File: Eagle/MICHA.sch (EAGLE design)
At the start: 57 parts, among them IC1 LM4041A12LP, K1 PIN20X2, T1 BSS84, U1 ARDUINO_MKR_ZERO, U2 MIKROE_CLICK, X1 RJ45-RJULE4318101, X2 RJ45-RJULE4318101, X3 RJ45-RJULE4318101, X4 RJ45-RJULE4318101, X5 RJ45-RJULE4318101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

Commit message: Downgrade to current version of PCB
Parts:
- R6, R7: value 15-1/4W -> 2k
- Z1, Z2: value 5,1V-1W -> 5,1V/1W
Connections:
- net SOL_HOT renamed SOL_WARM
- net VALVE1_DIR renamed VALVE1_CLOSE
- net VALVE1_POWER renamed VALVE1_OPEN
- net VALVE2_DIR renamed VALVE2_CLOSE
- net VALVE2_POWER renamed VALVE2_OPEN
- net D0: now also TBD2.6; no longer TBD2.4
- net D19: now also U1.A4; no longer U1.A1
- net D2: now also TBD2.4; no longer TBD2.6
- net D21: now also U1.A6; no longer U1.DAC0/A0
- net N$14: now also U1.A5; no longer U1.A2
- net THERMI1: now also U1.DAC0/A0; no longer U1.A3
- net THERMI2: now also U1.A1; no longer U1.A4
- net THERMI3: now also U1.A2; no longer U1.A5
- net THERMI4: now also U1.A3; no longer U1.A6
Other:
- moved on the sheet: AN, C1, C10, C11, C12, C13, C14, C15, C2, C3, C4, C5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

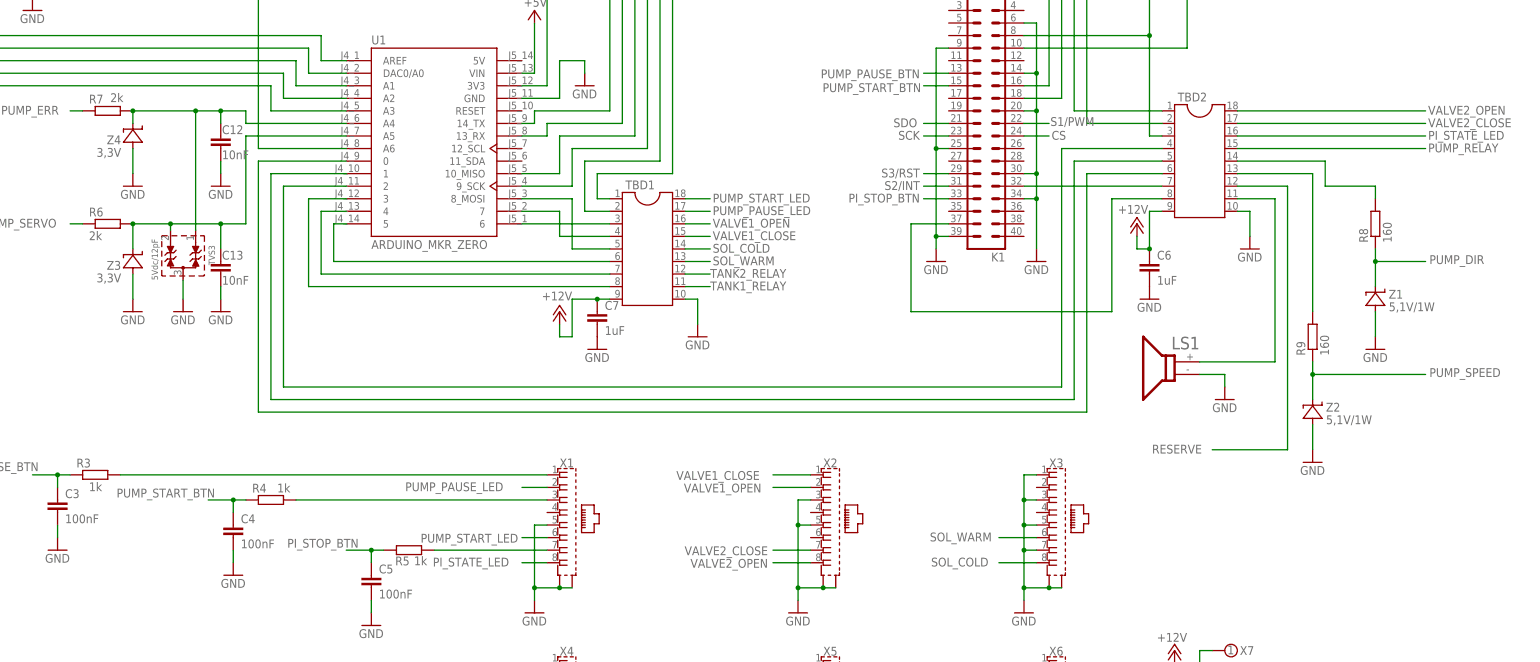
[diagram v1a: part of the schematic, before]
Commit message: Speed and power pump pins modified
- Voltage tags on X7
- Output valve names updated
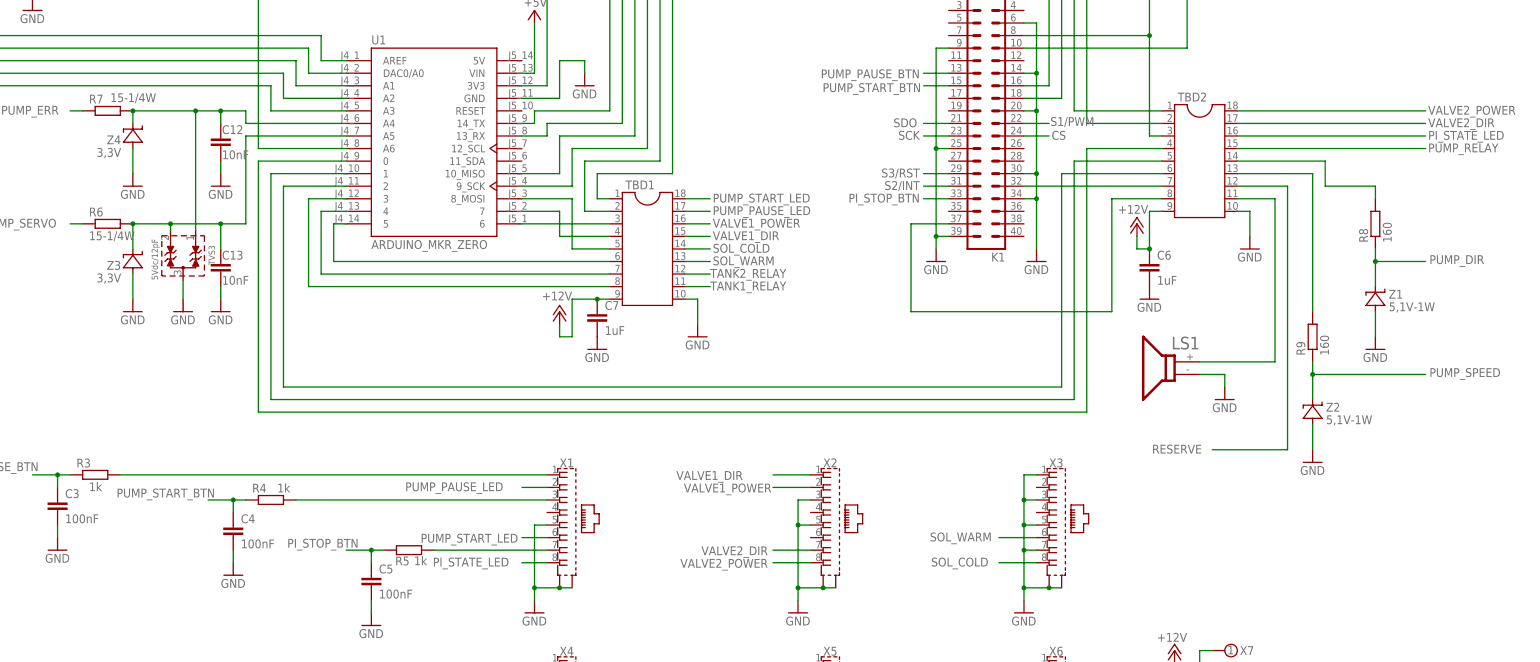
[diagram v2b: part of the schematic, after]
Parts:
- R6, R7: value 2k -> 15-1/4W
- Z1, Z2: value 5,1V/1W -> 5,1V-1W
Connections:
- net VALVE1_CLOSE renamed VALVE1_DIR
- net VALVE1_OPEN renamed VALVE1_POWER
- net VALVE2_CLOSE renamed VALVE2_DIR
- net VALVE2_OPEN renamed VALVE2_POWER
- net D0: now also TBD2.4; no longer TBD2.6
- net D2: now also TBD2.6; no longer TBD2.4
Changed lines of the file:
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@@
 <part name="GND9" library="supply1" deviceset="GND" device=""/>
 <part name="P+2" library="supply1" library_urn="urn:adsk.eagle:library:371" deviceset="+12V" device=""/>
-<part name="R6" library="resistor" deviceset="R-EU_" device="R1206" value="2k"/>
-<part name="R7" library="resistor" deviceset="R-EU_" device="R1206" value="2k"/>
+<part name="R6" library="resistor" deviceset="R-EU_" device="R1206" value="15-1/4W"/>
+<part name="R7" library="resistor" deviceset="R-EU_" device="R1206" value="15-1/4W"/>
 <part name="TBD2" library="ic-package" library_urn="urn:adsk.eagle:library:239" deviceset="DIL18" device="S" package3d_urn="urn:adsk.eagle:package:14434/1"/>
 <part name="GND12" library="supply1" deviceset="GND" device=""/>
@@
 <part name="GND39" library="supply1" deviceset="GND" device=""/>
 <part name="GND10" library="supply1" deviceset="GND" device=""/>
-<part name="Z1" library="Zener_SMA" deviceset="ZENER_SMA" device="" value="5,1V/1W"/>
-<part name="Z2" library="Zener_SMA" deviceset="ZENER_SMA" device="" value="5,1V/1W"/>
+<part name="Z1" library="Zener_SMA" deviceset="ZENER_SMA" device="" value="5,1V-1W"/>
+<part name="Z2" library="Zener_SMA" deviceset="ZENER_SMA" device="" value="5,1V-1W"/>
 <part name="Z3" library="Zener_SMA" deviceset="ZENER_SMA" device="" value="3,3V"/>
 <part name="Z4" library="Zener_SMA" deviceset="ZENER_SMA" device="" value="3,3V"/>
@@
 </segment>
 </net>
-<net name="VALVE1_OPEN" class="0">
+<net name="VALVE1_POWER" class="0">
 <segment>
 <wire x1="238.76" y1="106.68" x2="231.14" y2="106.68" width="0.1524" layer="91"/>
@@
 </segment>
 </net>
-<net name="VALVE1_CLOSE" class="0">
+<net name="VALVE1_DIR" class="0">
 <segment>
 <wire x1="238.76" y1="109.22" x2="231.14" y2="109.22" width="0.1524" layer="91"/>
@@
 </segment>
 </net>
-<net name="VALVE2_OPEN" class="0">
+<net name="VALVE2_POWER" class="0">
 <segment>
 <label x="363.728" y="182.118" size="1.778" layer="95"/>
@@
 </segment>
 </net>
-<net name="VALVE2_CLOSE" class="0">
+<net name="VALVE2_DIR" class="0">
 <segment>
 <label x="363.728" y="179.578" size="1.778" layer="95"/>
@@
 <pinref part="U1" gate="G$1" pin="0"/>
 <wire x1="127" y1="172.72" x2="144.78" y2="172.72" width="0.1524" layer="91"/>
-<pinref part="TBD2" gate="G$1" pin="6"/>
-<wire x1="309.88" y1="170.18" x2="294.64" y2="170.18" width="0.1524" layer="91"/>
-<wire x1="294.64" y1="170.18" x2="294.64" y2="121.92" width="0.1524" layer="91"/>
+<wire x1="294.64" y1="175.26" x2="294.64" y2="121.92" width="0.1524" layer="91"/>
+<pinref part="TBD2" gate="G$1" pin="4"/>
+<wire x1="294.64" y1="175.26" x2="309.88" y2="175.26" width="0.1524" layer="91"/>
 </segment>
 </net>
@@
 <pinref part="U1" gate="G$1" pin="2"/>
 <wire x1="132.08" y1="167.64" x2="144.78" y2="167.64" width="0.1524" layer="91"/>
-<pinref part="TBD2" gate="G$1" pin="4"/>
-<wire x1="309.88" y1="175.26" x2="289.56" y2="175.26" width="0.1524" layer="91"/>
-<wire x1="289.56" y1="175.26" x2="289.56" y2="127" width="0.1524" layer="91"/>
-</segment>
-</net>
+<wire x1="289.56" y1="127" x2="289.56" y2="170.18" width="0.1524" layer="91"/>
+<pinref part="TBD2" gate="G$1" pin="6"/>
+<wire x1="289.56" y1="170.18" x2="309.88" y2="170.18" width="0.1524" layer="91"/>
+</segment>
+</net>

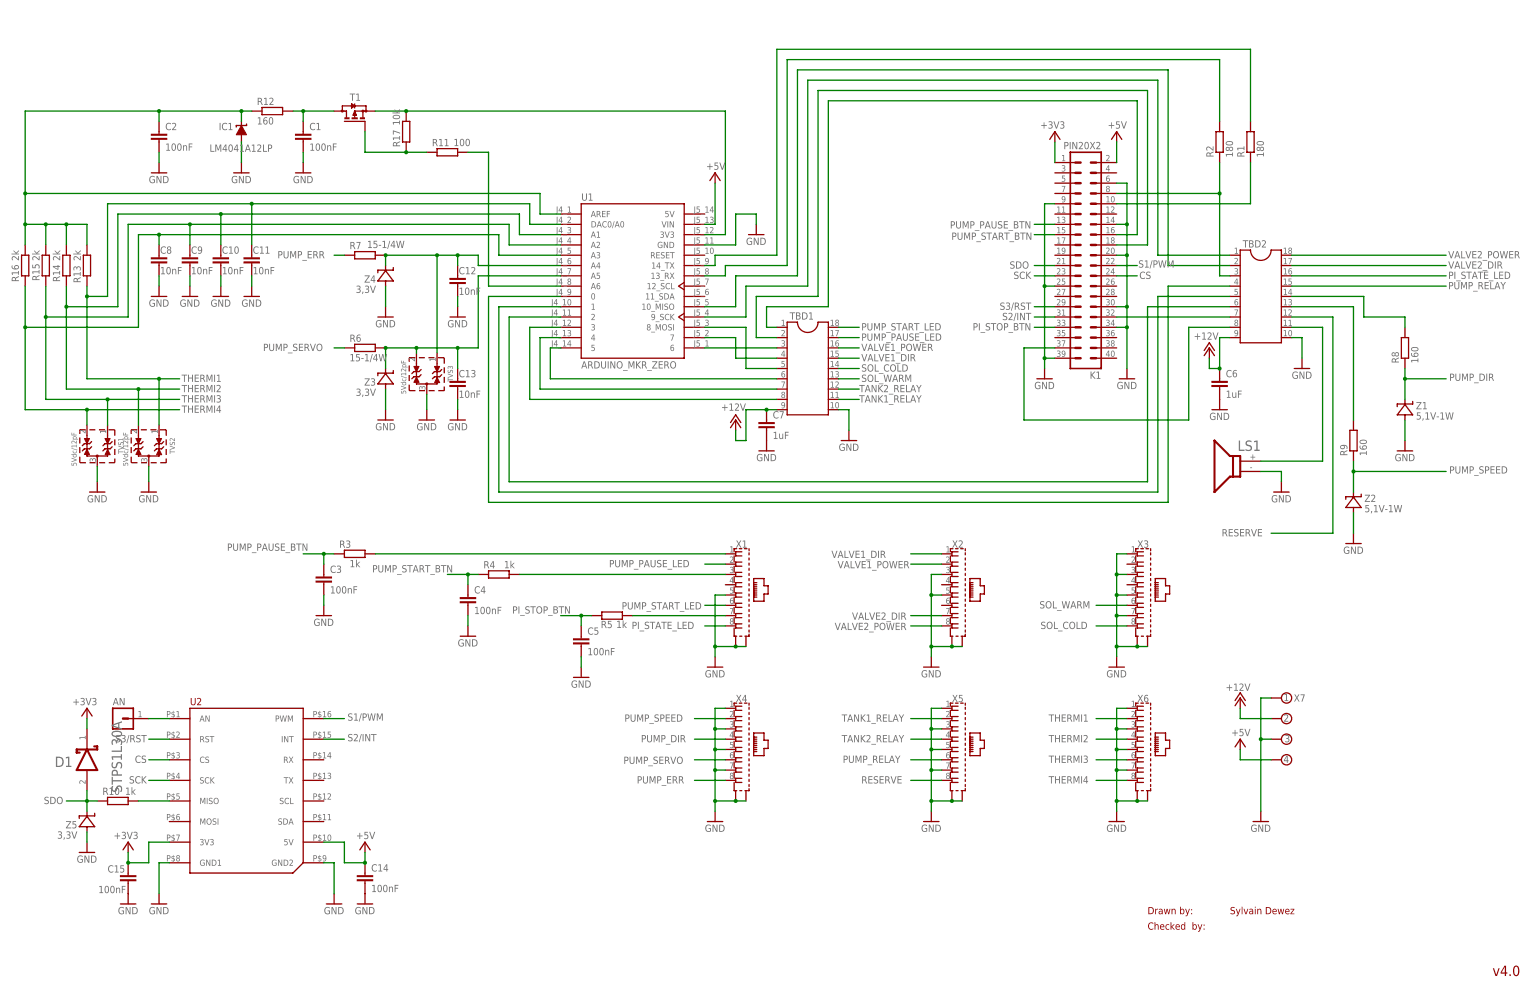
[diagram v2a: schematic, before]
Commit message: Pump servo pin updated
Modification of the next pins:
- Thermis power -> A0
- Error pump -> A1
- Servo pin -> A2
- Thermi 1 -> A3
- Thermi 2 -> A4
- Thermi 3 -> A5
- Thermi 4 -> A6
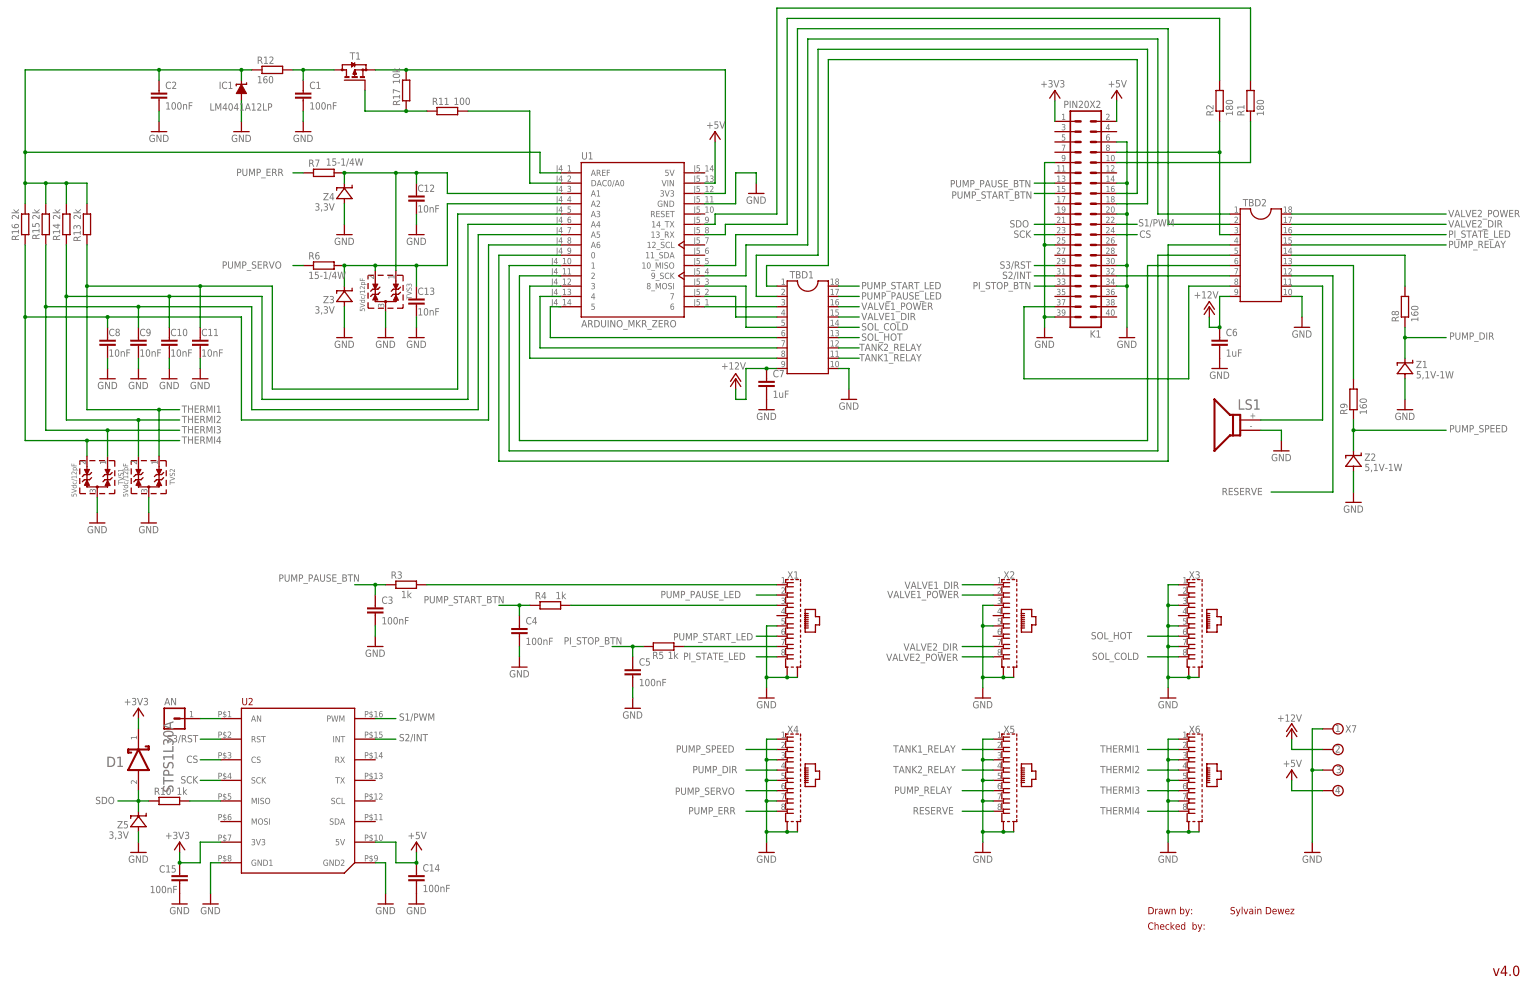
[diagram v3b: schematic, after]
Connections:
- net SOL_WARM renamed SOL_HOT
- net D19: now also U1.A1; no longer U1.A4
- net D21: now also U1.DAC0/A0; no longer U1.A6
- net N$14: now also U1.A2; no longer U1.A5
- net THERMI1: now also U1.A3; no longer U1.DAC0/A0
- net THERMI2: now also U1.A4; no longer U1.A1
- net THERMI3: now also U1.A5; no longer U1.A2
- net THERMI4: now also U1.A6; no longer U1.A3
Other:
- moved on the sheet: AN, C1, C10, C11, C12, C13, C14, C15, C2, C3, C4, C5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
